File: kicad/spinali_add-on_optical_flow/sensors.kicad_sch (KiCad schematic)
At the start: 4 parts, among them U1 AFBR-S50LX85D, U2 PAA3905E1, U3 ICM-45686, U4 ICM-42688-P

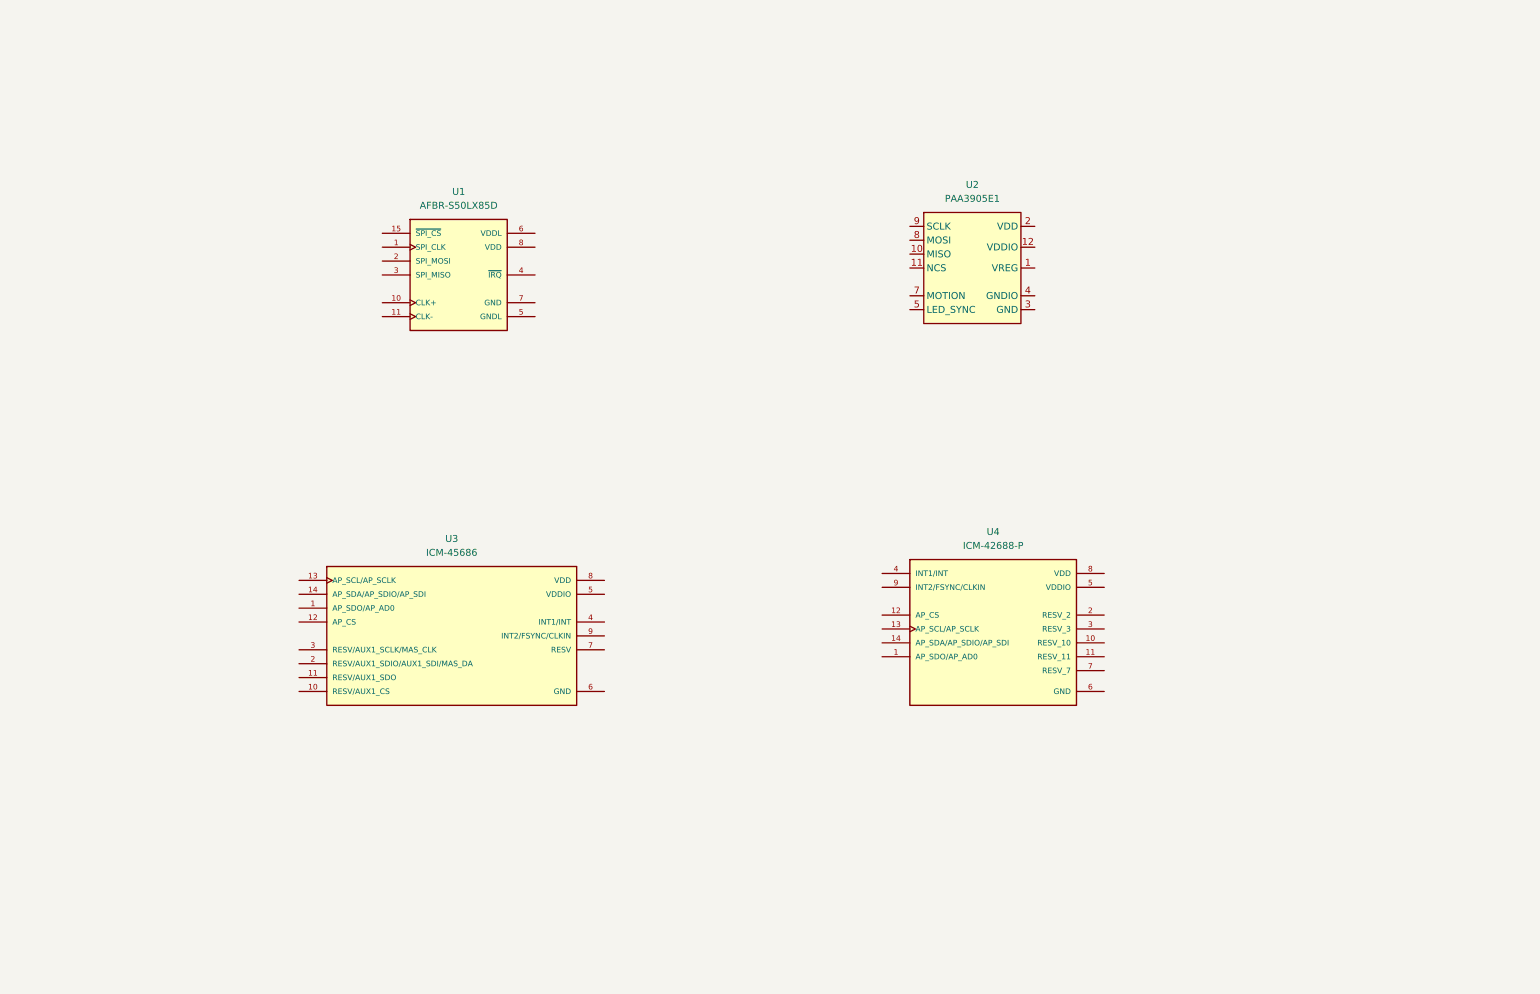
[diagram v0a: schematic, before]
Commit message: Updated schematic and started on layout
- Added LED driver circuit for PAA3905 LED_SYNC.
- Started on layouting PCB.
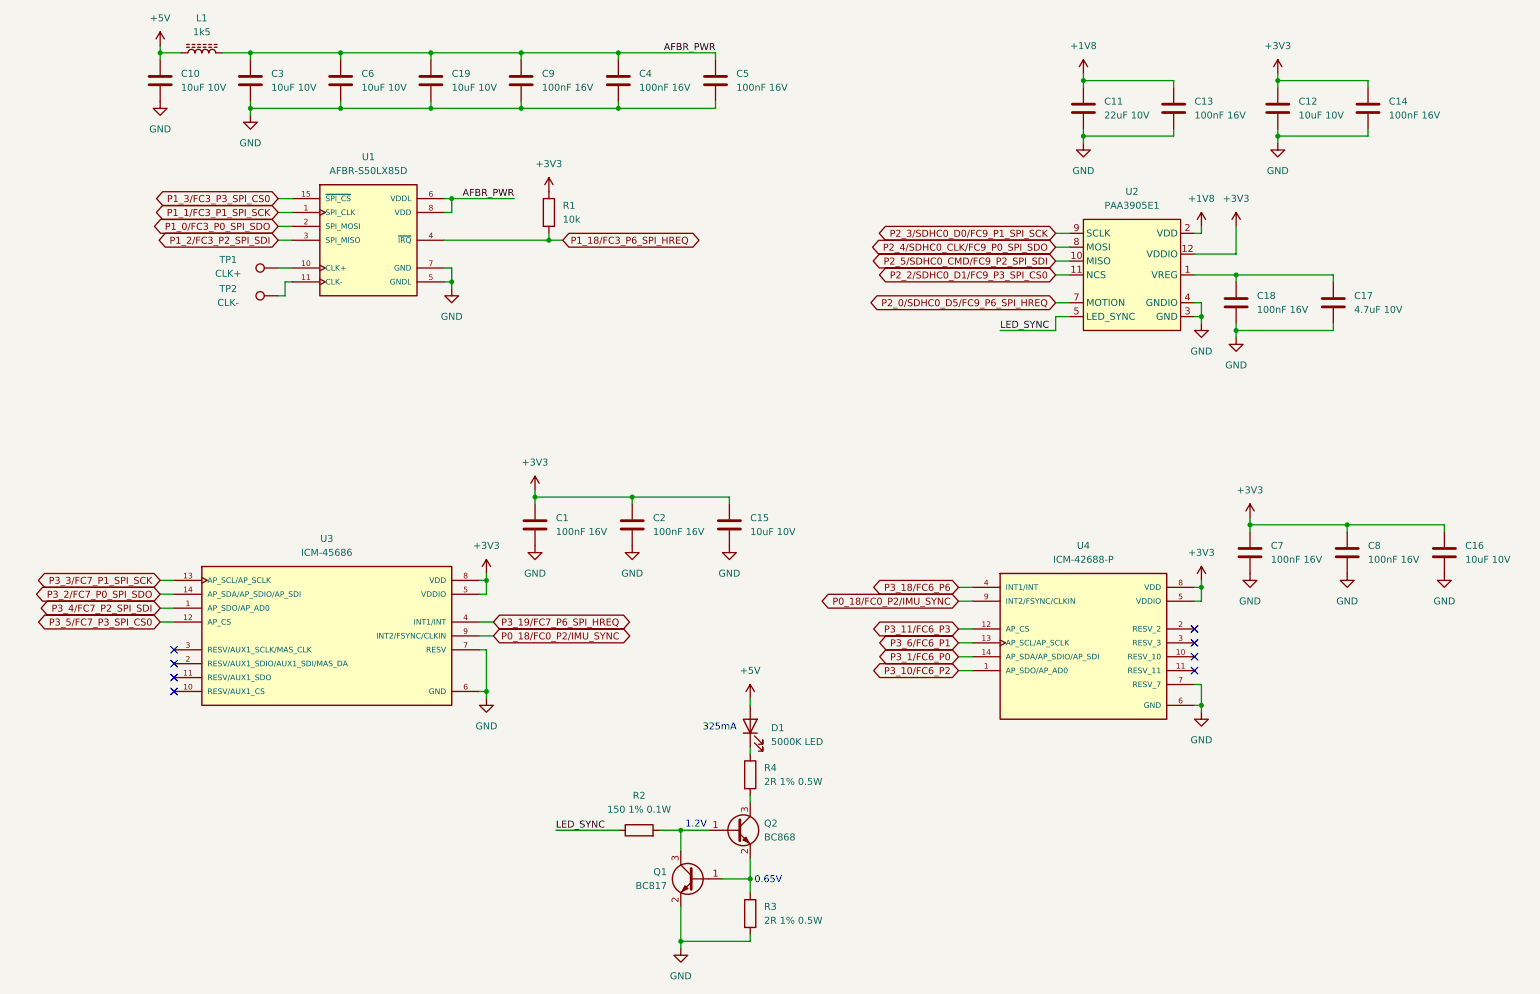
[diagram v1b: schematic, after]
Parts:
- added C1, C13, C14, C18, C2, C4, C5, C7, C8, C9: 100nF 16V, Capacitor_SMD:C_0402_1005Metric, symbol Device:C
- added C10, C12, C15, C16, C19, C3, C6: 10uF 10V, Capacitor_SMD:C_0805_2012Metric, symbol Device:C
- added C11: 22uF 10V, Capacitor_SMD:C_1206_3216Metric, symbol Device:C
- added C17: 4.7uF 10V, Capacitor_SMD:C_0603_1608Metric, symbol Device:C
- added D1: 5000K LED, Diodes:JK3030AWT-P-U50EA, symbol Device:LED
- added L1: 1k5, Inductor_SMD:L_0603_1608Metric, symbol Device:L_Ferrite
- added Q1: BC817, Package_TO_SOT_SMD:SOT-23, symbol Transistor_BJT:BC817
- added Q2: BC868, Package_TO_SOT_SMD:SOT-89-3, symbol Transistor_BJT:BC817
- added R1: 10k, Resistor_SMD:R_0402_1005Metric, symbol Device:R
- added R2: 150 1% 0.1W, Resistor_SMD:R_0603_1608Metric, symbol Device:R
- added R3, R4: 2R 1% 0.5W, Resistor_SMD:R_1210_3225Metric, symbol Device:R
- added TP1: CLK+, Connector_Wire:SolderWirePad_1x01_SMD_1x2mm, symbol Connector:TestPoint
- added TP2: CLK-, Connector_Wire:SolderWirePad_1x01_SMD_1x2mm, symbol Connector:TestPoint
- U1: DigiKey (none) -> 516-AFBR-S50LX85D-ND; MANUFACTURER Broadcom -> (none); MAXIMUM_PACKAGE_HEIGHT 7.7mm -> (none); MF (none) -> Broadcom Limited; MFPN (none) -> AFBR-S50LX85D; PARTREV September 17, 2020 -> (none); STANDARD IPC 2221B -> (none)
- U2: MF (none) -> Pixart
- U3: JLCPCB (none) -> C22459454; MF (none) -> TDK InvenSense; MFPN (none) -> ICM-45686
- U4: footprint Sensors:PQFN50P300X250X97-14N -> Sensors:IC_ICM-42688-P; JLCPCB (none) -> C1850418; MANUFACTURER TDK InvenSense -> (none); MAXIMUM_PACKAGE_HEIGHT 0.97mm -> (none); MF (none) -> TDK InvenSense; MFPN (none) -> ICM-42688-P; PARTREV 1.2 -> (none); STANDARD IPC-7351B -> (none)
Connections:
- net GND: now also U1.5 (GNDL), U2.3 (GND), U2.4 (GNDIO), U3.6 (GND), U3.7 (RESV), U4.6 (GND), U4.7 (RESV_7), C1.2, C10.2, C11.2, C12.2, C13.2, C14.2, C15.2, C16.2, C17.2, C18.2, C19.2, C2.2, C3.2, C4.2, C5.2, C6.2, C7.2, C8.2, C9.2, Q1.2 (E), R3.2
- net VDD: now also U1.6 (VDDL), C19.1, C3.1, C4.1, C5.1, C6.1, C9.1, L1.2
- net P1_1/FC3_P1_SPI_SCK: now reaches U1.1 (SPI_CLK)
- net at U1.10 (CLK+): now also TP1.1
- net at U1.11 (CLK-): now also TP2.1
- net P1_3/FC3_P3_SPI_CS0: now reaches U1.15 (~{SPI_CS})
- net P1_0/FC3_P0_SPI_SDO: now reaches U1.2 (SPI_MOSI)
- net P1_2/FC3_P2_SPI_SDI: now reaches U1.3 (SPI_MISO)
- net P1_18/FC3_P6_SPI_HREQ: now reaches U1.4 (~{IRQ})
- net P1_18/FC3_P6_SPI_HREQ: now also R1.2
- net at U2.1 (VREG): now also C17.1, C18.1
- net P2_5/SDHC0_CMD/FC9_P2_SPI_SDI: now reaches U2.10 (MISO)
- net P2_2/SDHC0_D1/FC9_P3_SPI_CS0: now reaches U2.11 (NCS)
- net +3V3: now reaches U2.12 (VDDIO)
- net +3V3: now also U3.5 (VDDIO), U3.8 (VDD), U4.5 (VDDIO), U4.8 (VDD), C1.1, C12.1, C14.1, C15.1, C16.1, C2.1, C7.1, C8.1, R1.1
- net +1V8: now reaches U2.2 (VDD)
- net +1V8: now also C11.1, C13.1
- net LED_SYNC: now reaches U2.5 (LED_SYNC)
- net LED_SYNC: now also R2.1
- net P2_0/SDHC0_D5/FC9_P6_SPI_HREQ: now reaches U2.7 (MOTION)
- net P2_4/SDHC0_CLK/FC9_P0_SPI_SDO: now reaches U2.8 (MOSI)
- net P2_3/SDHC0_D0/FC9_P1_SPI_SCK: now reaches U2.9 (SCLK)
- net P3_10/FC6_P2: now reaches U4.1 (AP_SDO/AP_AD0)
- net P3_11/FC6_P3: now reaches U4.12 (AP_CS)
- net P3_6/FC6_P1: now reaches U4.13 (AP_SCL/AP_SCLK)
- net P3_1/FC6_P0: now reaches U4.14 (AP_SDA/AP_SDIO/AP_SDI)
- net P3_18/FC6_P6: now reaches U4.4 (INT1/INT)
- net P0_18/FC0_P2/IMU_SYNC: now reaches U4.9 (INT2/FSYNC/CLKIN)
- net P0_18/FC0_P2/IMU_SYNC: now also U3.9 (INT2/FSYNC/CLKIN)
- net P3_4/FC7_P2_SPI_SDI: now reaches U3.1 (AP_SDO/AP_AD0)
- net P3_5/FC7_P3_SPI_CS0: now reaches U3.12 (AP_CS)
- net P3_3/FC7_P1_SPI_SCK: now reaches U3.13 (AP_SCL/AP_SCLK)
- net P3_2/FC7_P0_SPI_SDO: now reaches U3.14 (AP_SDA/AP_SDIO/AP_SDI)
- net P3_19/FC7_P6_SPI_HREQ: now reaches U3.4 (INT1/INT)
- new net: D1.1 (K), R4.1
- new net: Q2.3 (C), R4.2
- new net: Q1.3 (C), Q2.1 (B), R2.2
- new net: Q1.1 (B), Q2.2 (E), R3.1
- new net +5V: C10.1, D1.2 (A), L1.1
- no-connect marks 0 -> 8
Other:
- note added: "0.65V"
- note added: "1.2V"
- note added: "325mA"
- moved on the sheet: U1, U2, U3, U4

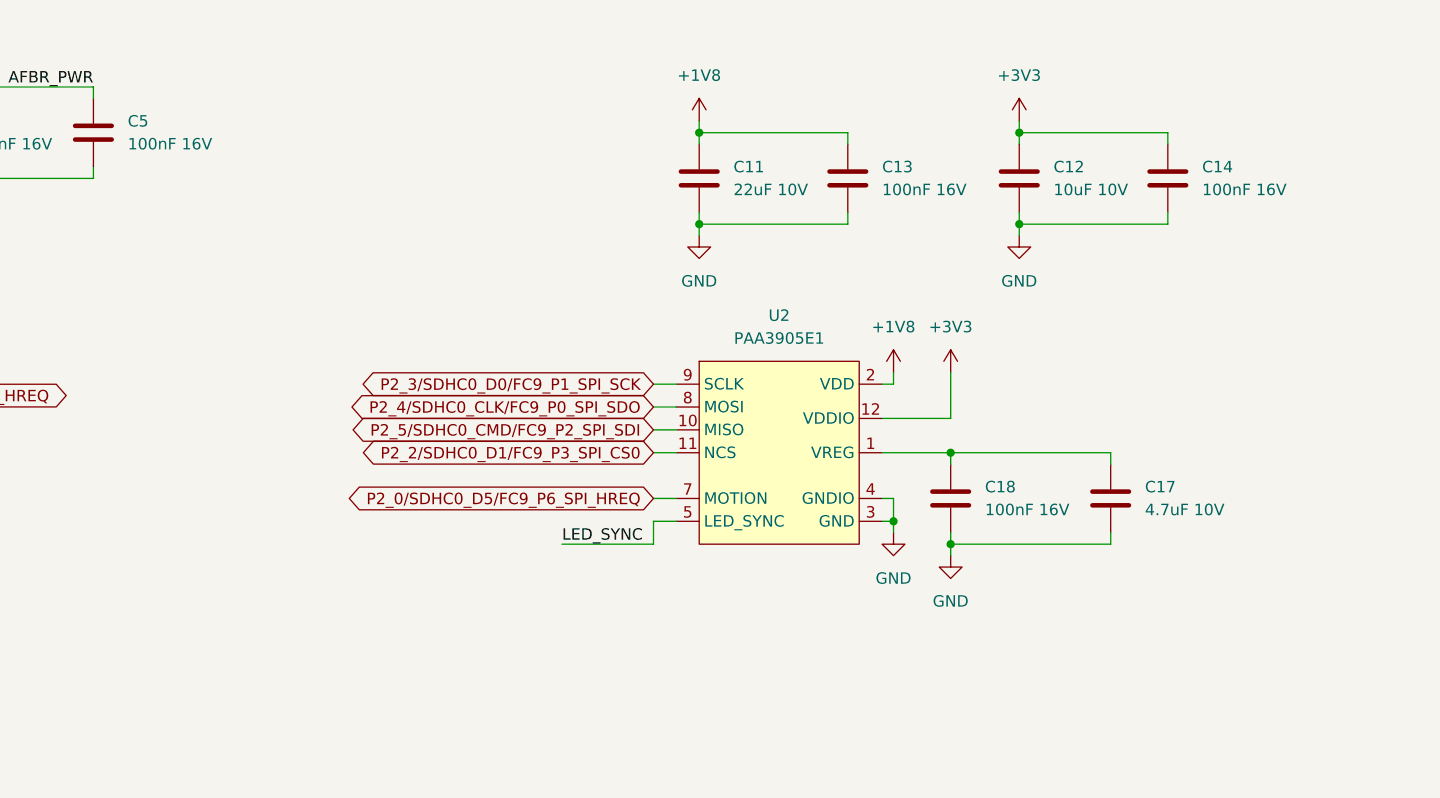
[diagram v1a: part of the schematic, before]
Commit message: Finished layout and schematic
- Added cognipilot logo to silkscreen.
- Added test points to PAA3905E1 data signals.
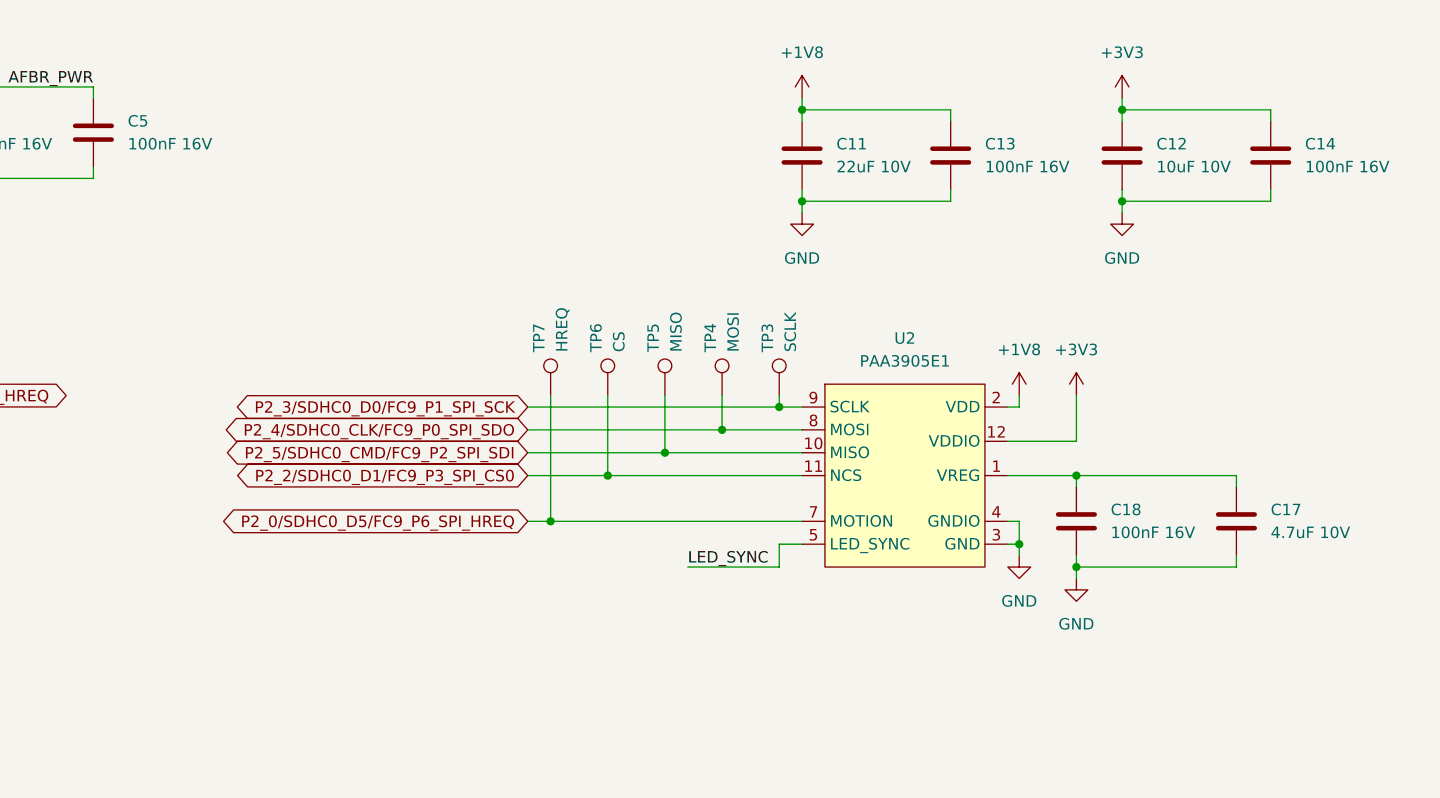
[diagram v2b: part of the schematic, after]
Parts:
- added TP3: SCLK, TestPoint:TestPoint_Pad_D1.0mm, symbol Connector:TestPoint
- added TP4: MOSI, TestPoint:TestPoint_Pad_D1.0mm, symbol Connector:TestPoint
- added TP5: MISO, TestPoint:TestPoint_Pad_D1.0mm, symbol Connector:TestPoint
- added TP6: CS, TestPoint:TestPoint_Pad_D1.0mm, symbol Connector:TestPoint
- added TP7: HREQ, TestPoint:TestPoint_Pad_D1.0mm, symbol Connector:TestPoint
- C1, C13, C14, C18, C2, C4, C5, C7, C8, C9: DigiKey (none) -> 1276-1001-1-ND
- C10, C12, C15, C16, C19, C3, C6: DigiKey (none) -> 490-14381-1-ND
- C11: DigiKey (none) -> 490-5309-1-ND
- C17: DigiKey (none) -> 490-GRM188Z71C475KE21DCT-ND
- L1: DigiKey (none) -> 490-5216-1-ND
- Q1: DigiKey (none) -> 1727-2919-1-ND; MF (none) -> Nexperia USA Inc.; MFPN (none) -> BC817-40,215
- R1: DigiKey (none) -> YAG3436CT-ND
- TP1, TP2: now left out of the parts list
- U3: DigiKey (none) -> 1428-ICM-45686CT-ND
- U4: DigiKey (none) -> 1428-ICM-42688-PCT-ND
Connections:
- net P2_0/SDHC0_D5/FC9_P6_SPI_HREQ: now also TP7.1
- net P2_2/SDHC0_D1/FC9_P3_SPI_CS0: now also TP6.1
- net P2_3/SDHC0_D0/FC9_P1_SPI_SCK: now also TP3.1
- net P2_4/SDHC0_CLK/FC9_P0_SPI_SDO: now also TP4.1
- net P2_5/SDHC0_CMD/FC9_P2_SPI_SDI: now also TP5.1
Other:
- moved on the sheet: C11, C12, C13, C14, C17, C18, U2
